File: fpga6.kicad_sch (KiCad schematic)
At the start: 92 parts

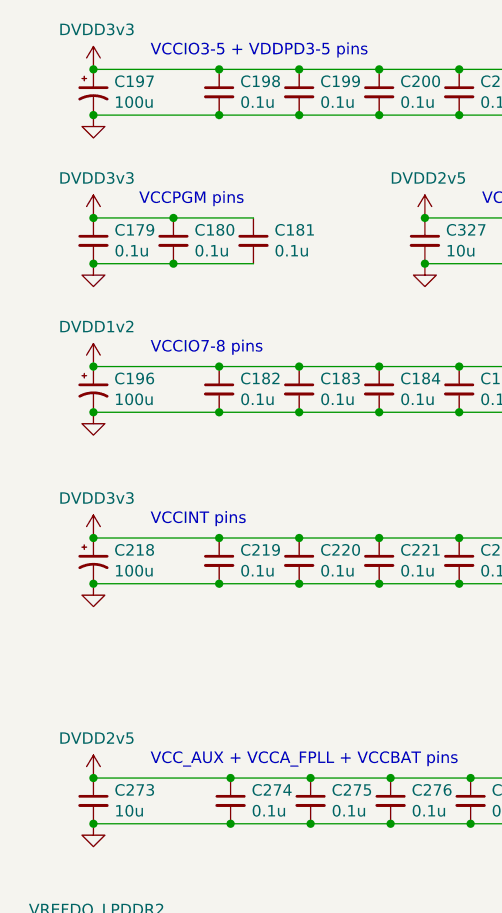
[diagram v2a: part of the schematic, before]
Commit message: fix power supply connections on v1.6 schematic
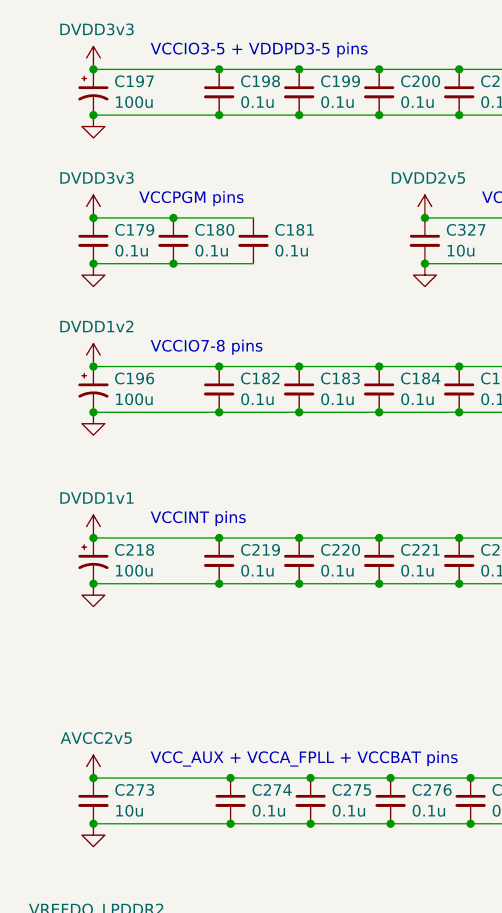
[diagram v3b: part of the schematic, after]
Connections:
- net DVDD2v5: no longer C273.1, C274.1, C275.1, C276.1, C277.1, C278.1, C279.1, C280.1, C281.1, C282.1, C283.1, C284.1, C285.1, C326.1
- net DVDD3v3: no longer C218.1, C219.1, C220.1, C221.1, C222.1, C223.1, C224.1, C225.1, C226.1, C227.1, C228.1, C229.1, C230.1, C231.1, C232.1, C233.1, C234.1, C235.1, C236.1, C237.1, C238.1, C239.1, C240.1, C241.1, C242.1, C243.1, C244.1
- new net AVCC2v5: C273.1, C274.1, C275.1, C276.1, C277.1, C278.1, C279.1, C280.1, C281.1, C282.1, C283.1, C284.1, C285.1, C326.1
- new net DVDD1v1: C218.1, C219.1, C220.1, C221.1, C222.1, C223.1, C224.1, C225.1, C226.1, C227.1, C228.1, C229.1, C230.1, C231.1, C232.1, C233.1, C234.1, C235.1, C236.1, C237.1, C238.1, C239.1, C240.1, C241.1, C242.1, C243.1, C244.1
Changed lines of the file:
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@@
 (kicad_sch
-	(version 20231120)
+	(version 20250114)
 	(generator "eeschema")
-	(generator_version "8.0")
+	(generator_version "9.0")
 	(paper "A4")
 	(title_block
@@
 		(rev "1.6")
 	)
+	(text "VCCIO7-8 pins"
+		(exclude_from_sim no)
+		(at 30.48 60.96 0)
+		(effects
+			(font
+				(size 1.27 1.27)
+			)
+			(justify left bottom)
+		)
+	)
+	(text "VREFB7-8 pins"
+		(exclude_from_sim no)
+		(at 29.21 125.73 0)
+		(effects
+			(font
+				(size 1.27 1.27)
+			)
+			(justify left bottom)
+		)
+	)
+	(text "VCCPD7-8 pins"
+		(exclude_from_sim no)
+		(at 67.31 44.45 0)
+		(effects
+			(font
+				(size 1.27 1.27)
+			)
+			(justify left bottom)
+		)
+	)
+	(text "VCCINT pins"
+		(exclude_from_sim no)
+		(at 30.48 80.01 0)
+		(effects
+			(font
+				(size 1.27 1.27)
+			)
+			(justify left bottom)
+		)
+	)
+	(text "VCCPGM pins"
+		(exclude_from_sim no)
+		(at 29.21 44.45 0)
+		(effects
+			(font
+				(size 1.27 1.27)
+			)
+			(justify left bottom)
+		)
+	)
+	(text "VCCIO3-5 + VDDPD3-5 pins"
+		(exclude_from_sim no)
+		(at 30.48 27.94 0)
+		(effects
+			(font
+				(size 1.27 1.27)
+			)
+			(justify left bottom)
+		)
+	)
+	(text "VCC_AUX + VCCA_FPLL + VCCBAT pins"
+		(exclude_from_sim no)
+		(at 30.48 106.68 0)
+		(effects
+			(font
+				(size 1.27 1.27)
+			)
+			(justify left bottom)
+		)
+	)
 	(junction
 		(at 100.33 67.31)
@@
 		)
 	)
-	(text "VCCIO7-8 pins"
-		(exclude_from_sim no)
-		(at 30.48 60.96 0)
-		(effects
-			(font
-				(size 1.27 1.27)
-			)
-			(justify left bottom)
-		)
-	)
-	(text "VREFB7-8 pins"
-		(exclude_from_sim no)
-		(at 29.21 125.73 0)
-		(effects
-			(font
-				(size 1.27 1.27)
-			)
-			(justify left bottom)
-		)
-	)
-	(text "VCCPD7-8 pins"
-		(exclude_from_sim no)
-		(at 67.31 44.45 0)
-		(effects
-			(font
-				(size 1.27 1.27)
-			)
-			(justify left bottom)
-		)
-	)
-	(text "VCCINT pins"
-		(exclude_from_sim no)
-		(at 30.48 80.01 0)
-		(effects
-			(font
-				(size 1.27 1.27)
-			)
-			(justify left bottom)
-		)
-	)
-	(text "VCCPGM pins"
-		(exclude_from_sim no)
-		(at 29.21 44.45 0)
-		(effects
-			(font
-				(size 1.27 1.27)
-			)
-			(justify left bottom)
-		)
-	)
-	(text "VCCIO3-5 + VDDPD3-5 pins"
-		(exclude_from_sim no)
-		(at 30.48 27.94 0)
-		(effects
-			(font
-				(size 1.27 1.27)
-			)
-			(justify left bottom)
-		)
-	)
-	(text "VCC_AUX + VCCA_FPLL + VCCBAT pins"
-		(exclude_from_sim no)
-		(at 30.48 106.68 0)
-		(effects
-			(font
-				(size 1.27 1.27)
-			)
-			(justify left bottom)
-		)
-	)
 	(symbol
 		(lib_id "Device:CP1_Small")
@@
 			)
 		)
-		(property "Value" "DVDD3v3"
+		(property "Value" "DVDD1v1"
 			(at 24.511 76.8858 0)
 			(effects
@@
 			)
 		)
-		(property "Value" "DVDD2v5"
+		(property "Value" "AVCC2v5"
 			(at 24.511 103.5558 0)
 			(effects
